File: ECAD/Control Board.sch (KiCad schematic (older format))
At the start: 69 parts, among them J3 Thermocouple, J4 SD_Card, J5 PWR/Heat, J6 FAN, J7 UPDI, Q1 IPD50N06S4L08, Q2 IPD50N06S4L08, SW1 Reflow, SW2 Stop, SW3 Set temp mode, U1 ATtiny1614-SS, U2 LD1086DT33, U3 AD8497, U4 HT16K33, U5 LT3012

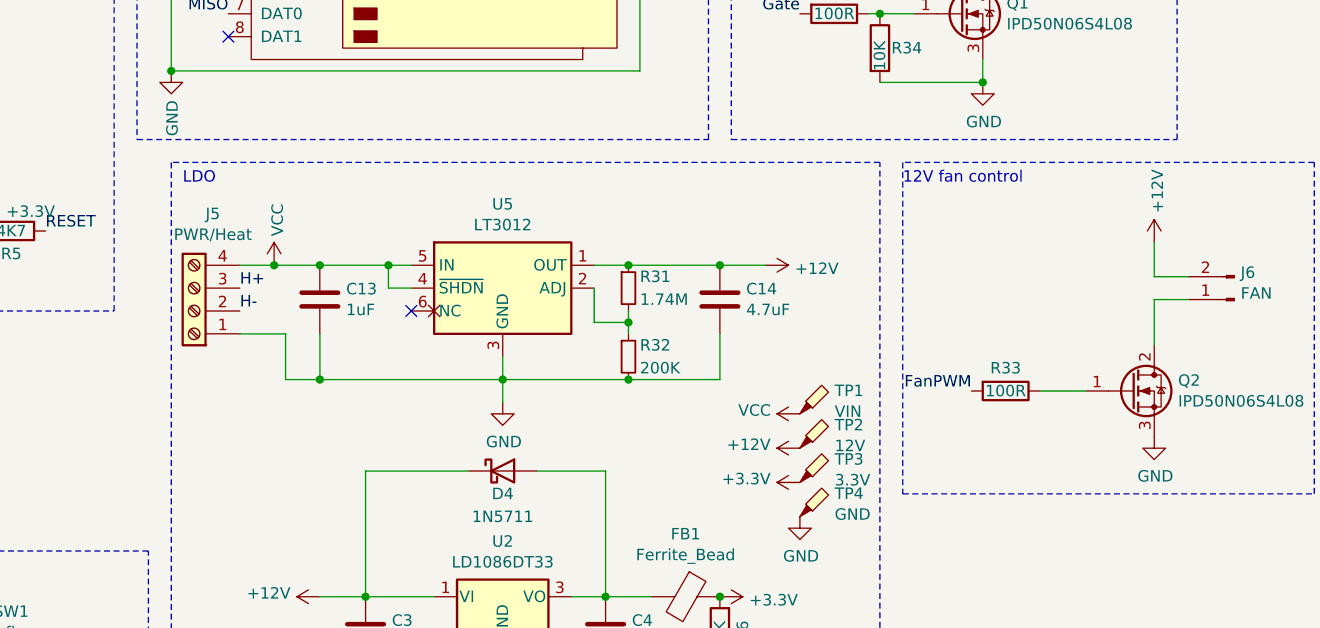
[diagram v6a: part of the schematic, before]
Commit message: Replaced primary LDO with LM317
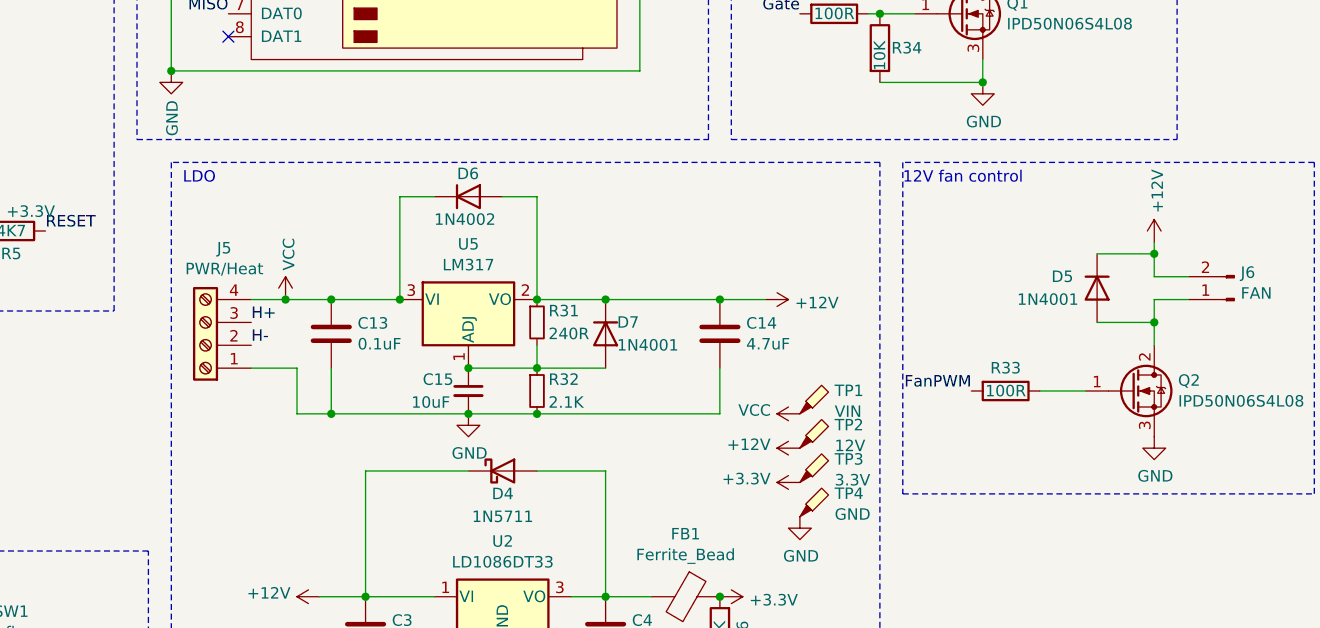
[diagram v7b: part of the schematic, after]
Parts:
- removed U5: LT3012, PCB Heater:Linear_Technology-LT3012EFETRPBF-Level_B, symbol Regulators:LT3012
- added C15: 10uF, Capacitor_SMD:C_0805_2012Metric_Pad1.18x1.45mm_HandSolder, symbol Device:C_Small
- added D5, D7: 1N4001, Diode_THT:D_T-1_P5.08mm_Horizontal, symbol Device:D
- added D6: 1N4002, Diode_THT:D_T-1_P5.08mm_Horizontal, symbol Device:D
- added U5: LM317, Package_TO_SOT_THT:TO-220-3_Vertical, symbol Regulator_Linear:LM317_TO-220
- C13: value 1uF -> 0.1uF
- R31: value 1.74M -> 240R
- R32: value 200K -> 2.1K
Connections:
- net +12V: now also D5.1 (K), D6.2 (A), D7.1 (K), U5.2 (VO)
- net GND: now also C15.2
- net VCC: now also D6.1 (K), U5.3 (VI)
- net at R31.2, R32.1: now also C15.1, D7.2 (A), U5.1 (ADJ)
- net at J6.1 (Pin_1), Q2.2 (D): now also D5.2 (A)
- no-connect marks 10 -> 9
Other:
- moved on the sheet: C13, C14, J5, R31, R32

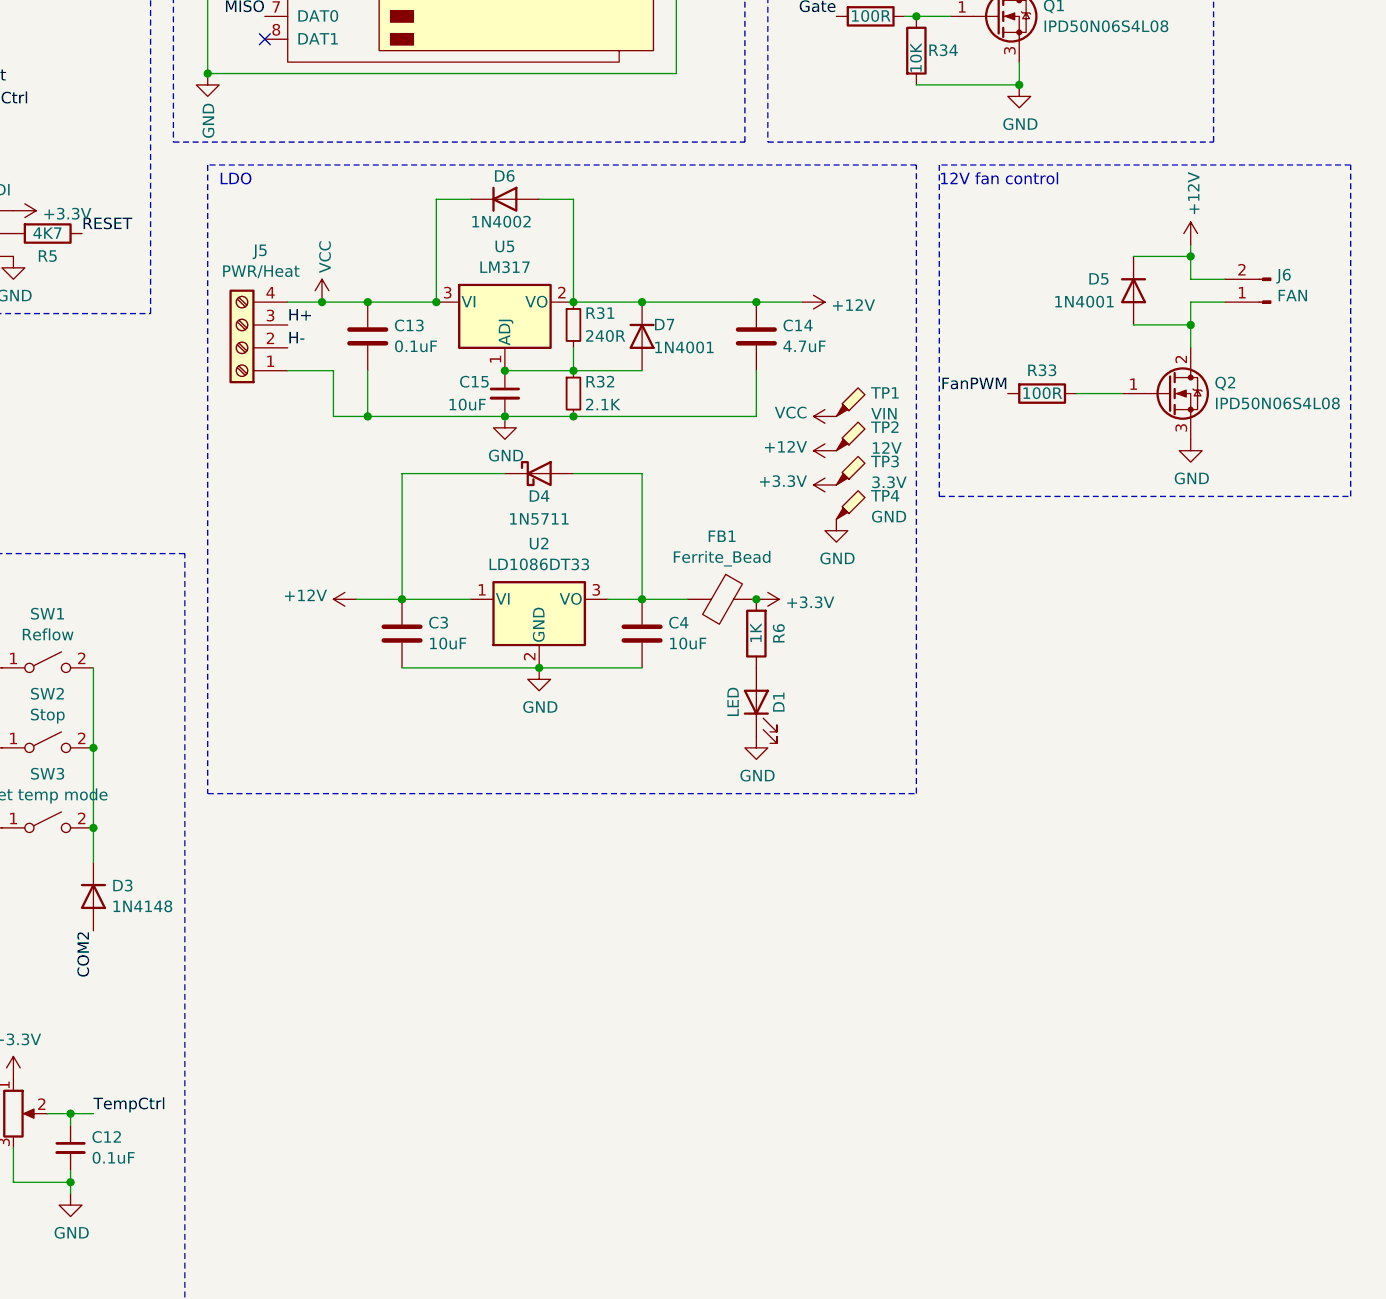
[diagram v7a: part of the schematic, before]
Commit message: Replaced linear regulator with switching regulator
Chose switching regulator for the sake of less heat. Undecided as to whether I will end up using a premade module or incorporating the circuitry

Replaced 12V rail with 5V rail, to increase efficiency of the LDO. Requires a 5V fan now.

Bumped revision number to 0.4
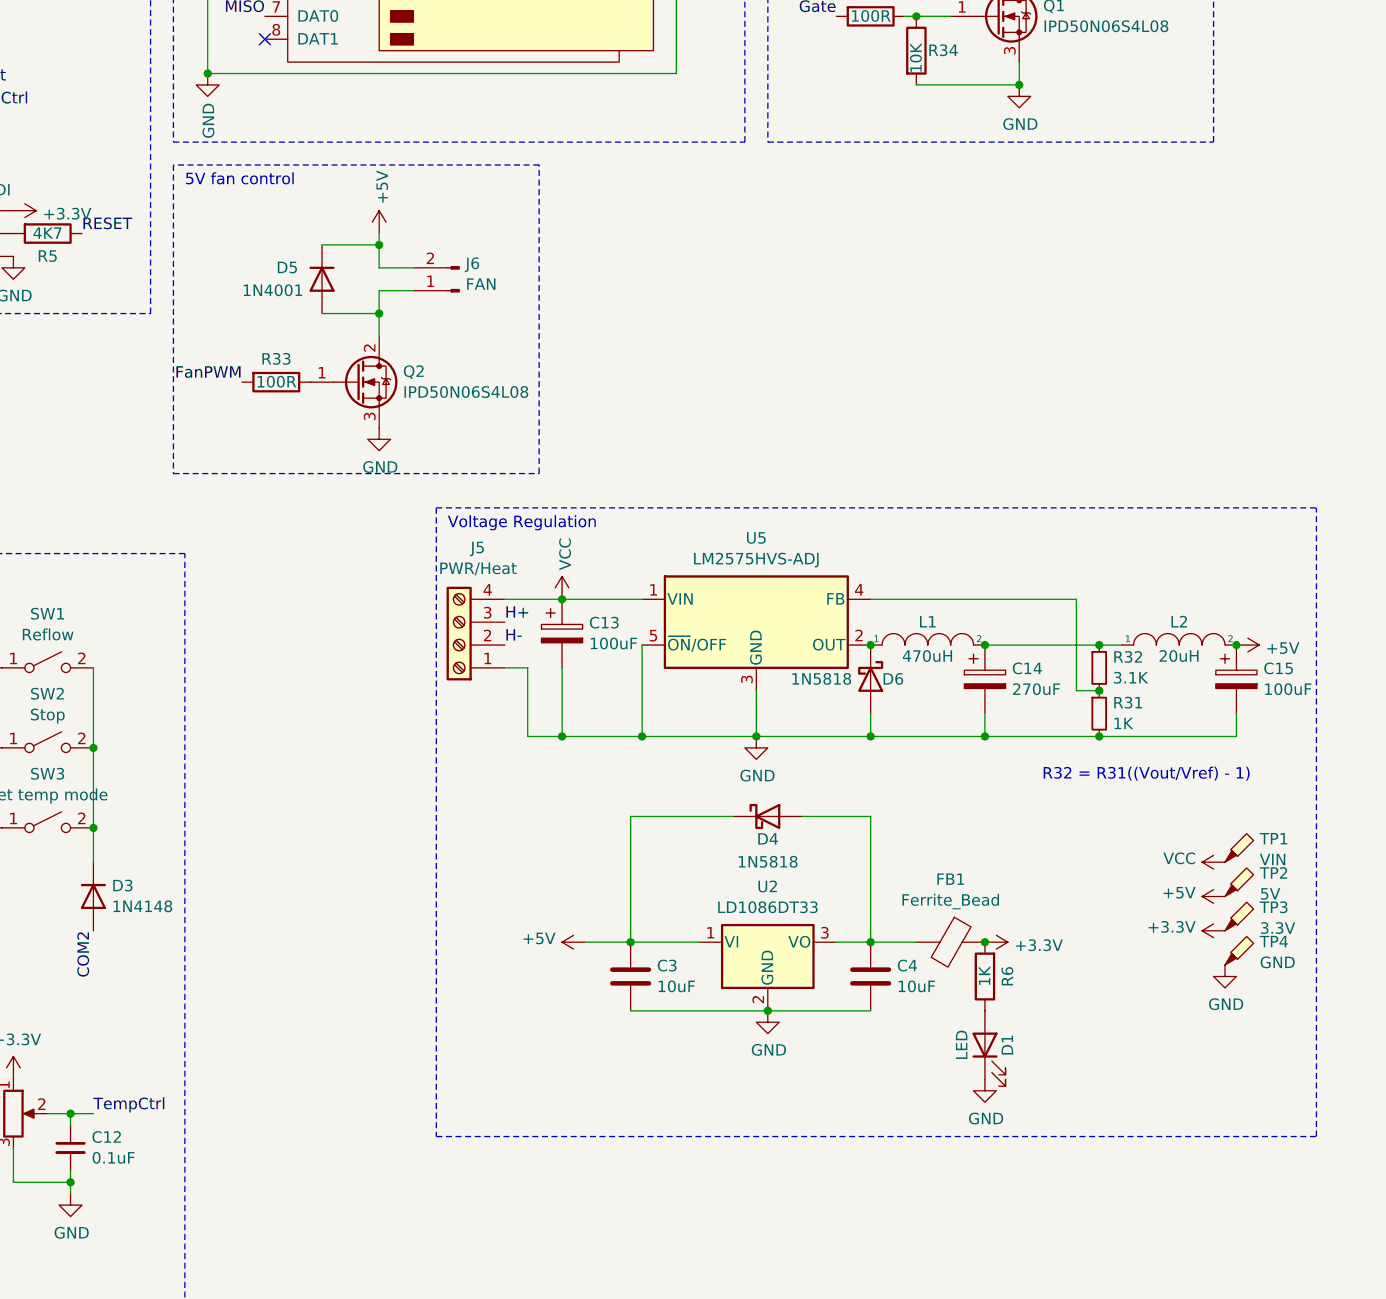
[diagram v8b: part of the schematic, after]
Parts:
- removed C13: 0.1uF, Capacitor_SMD:C_0805_2012Metric_Pad1.18x1.45mm_HandSolder, symbol Device:C
- removed C14: 4.7uF, Capacitor_SMD:C_0805_2012Metric_Pad1.18x1.45mm_HandSolder, symbol Device:C
- removed C15: 10uF, Capacitor_SMD:C_0805_2012Metric_Pad1.18x1.45mm_HandSolder, symbol Device:C_Small
- removed D6: 1N4002, Diode_THT:D_T-1_P5.08mm_Horizontal, symbol Device:D
- removed D7: 1N4001, Diode_THT:D_T-1_P5.08mm_Horizontal, symbol Device:D
- removed U5: LM317, Package_TO_SOT_THT:TO-220-3_Vertical, symbol Regulator_Linear:LM317_TO-220
- added C13, C15: 100uF, symbol Device:CP
- added C14: 270uF, symbol Device:CP
- added D6: 1N5818, Diode_THT:D_T-1_P5.08mm_Horizontal, symbol Device:D_Schottky
- added L1: 470uH, symbol pspice:INDUCTOR
- added L2: 20uH, symbol pspice:INDUCTOR
- added U5: LM2575HVS-ADJ, Package_TO_SOT_SMD:TO-263-5_TabPin3, symbol Regulator_Switching:LM2575-12BU
- D4: value 1N5711 -> 1N5818
- R31: value 240R -> 1K
- R32: value 2.1K -> 3.1K
- TP2: value 12V -> 5V
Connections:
- net GND: now also R31.2, C13.2, C14.2, C15.2, D6.2 (A), U5.3 (GND), U5.5 (~ON~/OFF); no longer R32.2
- net VCC: now also C13.1, U5.1 (VIN)
- net at R32.1: now also C14.1, L1.2, L2.1; no longer R31.2
- net +12V renamed +5V
- net +5V: now also C15.1, L2.2; no longer R31.1
- new net: D6.1 (K), L1.1, U5.2 (OUT)
- new net: R31.1, R32.2, U5.4 (FB)
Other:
- note added: "5V fan control"
- note added: "R32 = R31((Vout/Vref) - 1)"
- note added: "Voltage Regulation\n"
- note removed: "12V fan control"
- note removed: "LDO"
- moved on the sheet: C3, C4, D1, D4, D5, FB1, J5, J6, Q2, R33, R6, TP1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
